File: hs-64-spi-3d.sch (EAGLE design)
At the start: 30 parts, among them J1 DF40C-70DP-0.4V(51), J2 A79622-001, U1 RHD2064_BGA, U2 BNO055, U3 TLV70725

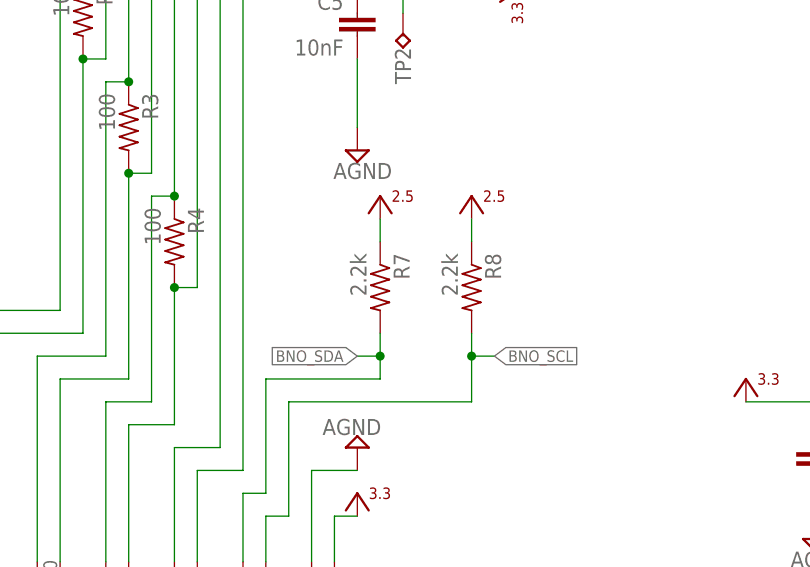
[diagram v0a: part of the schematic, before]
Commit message: Decreased I2C pull-up resistors to 2k.
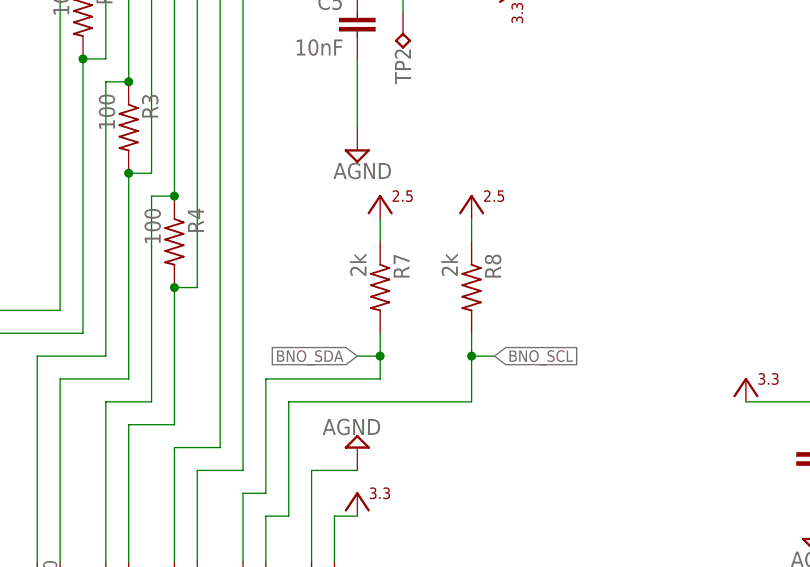
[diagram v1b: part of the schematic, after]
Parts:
- R7, R8: value 2.2k -> 2k
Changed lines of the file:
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@@
 <part name="P7" library="jonnew" deviceset="+3V3" device=""/>
 <part name="U$2" library="jonnew" deviceset="+2V5" device=""/>
-<part name="R7" library="jonnew" deviceset="R" device="_0201T" value="2.2k"/>
-<part name="R8" library="jonnew" deviceset="R" device="_0201T" value="2.2k"/>
+<part name="R7" library="jonnew" deviceset="R" device="_0201T" value="2k"/>
+<part name="R8" library="jonnew" deviceset="R" device="_0201T" value="2k"/>
 <part name="U$3" library="jonnew" deviceset="+2V5" device=""/>
 <part name="U$4" library="jonnew" deviceset="+2V5" device=""/>

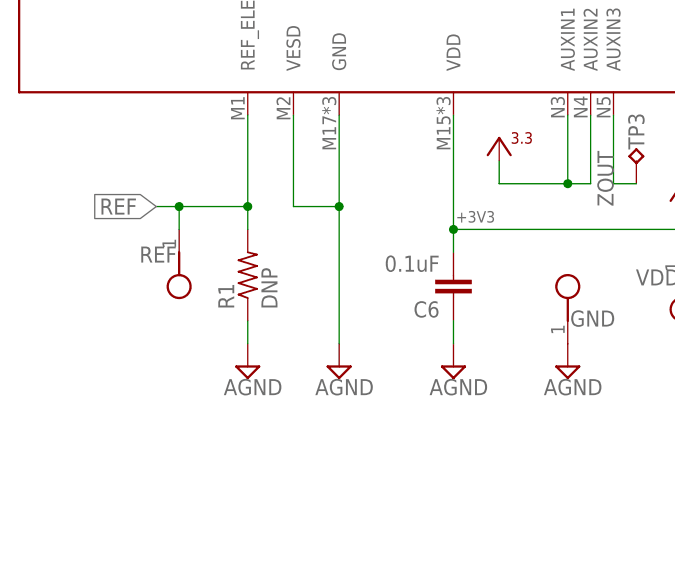
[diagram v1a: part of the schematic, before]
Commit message: Connection between REF to GND is now done by default.
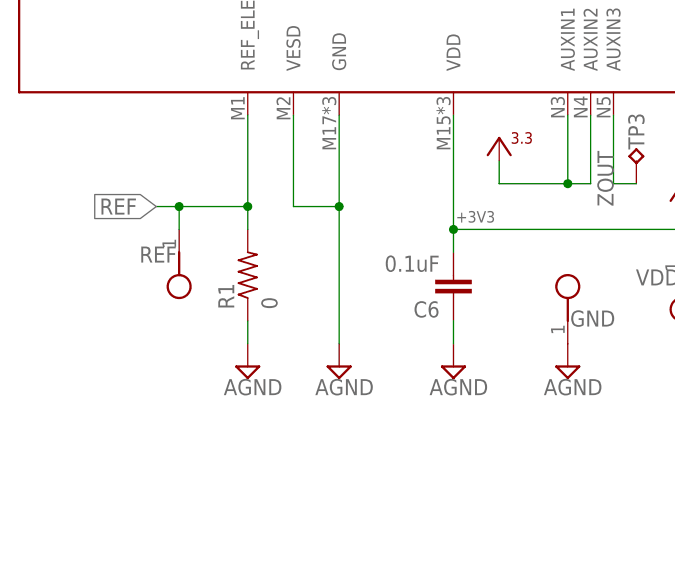
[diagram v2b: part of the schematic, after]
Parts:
- R1: value DNP -> 0
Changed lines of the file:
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@@
 <part name="SUPPLY1" library="jonnew" deviceset="AGND" device=""/>
 <part name="J2" library="hs-64-spi" deviceset="A79622-001" device=""/>
-<part name="R1" library="jonnew" deviceset="R" device="_0603" value="DNP"/>
+<part name="R1" library="jonnew" deviceset="R" device="_0603" value="0"/>
 <part name="SUPPLY11" library="jonnew" deviceset="AGND" device=""/>
 <part name="C7" library="jonnew" deviceset="C" device="_0402" value="1u"/>

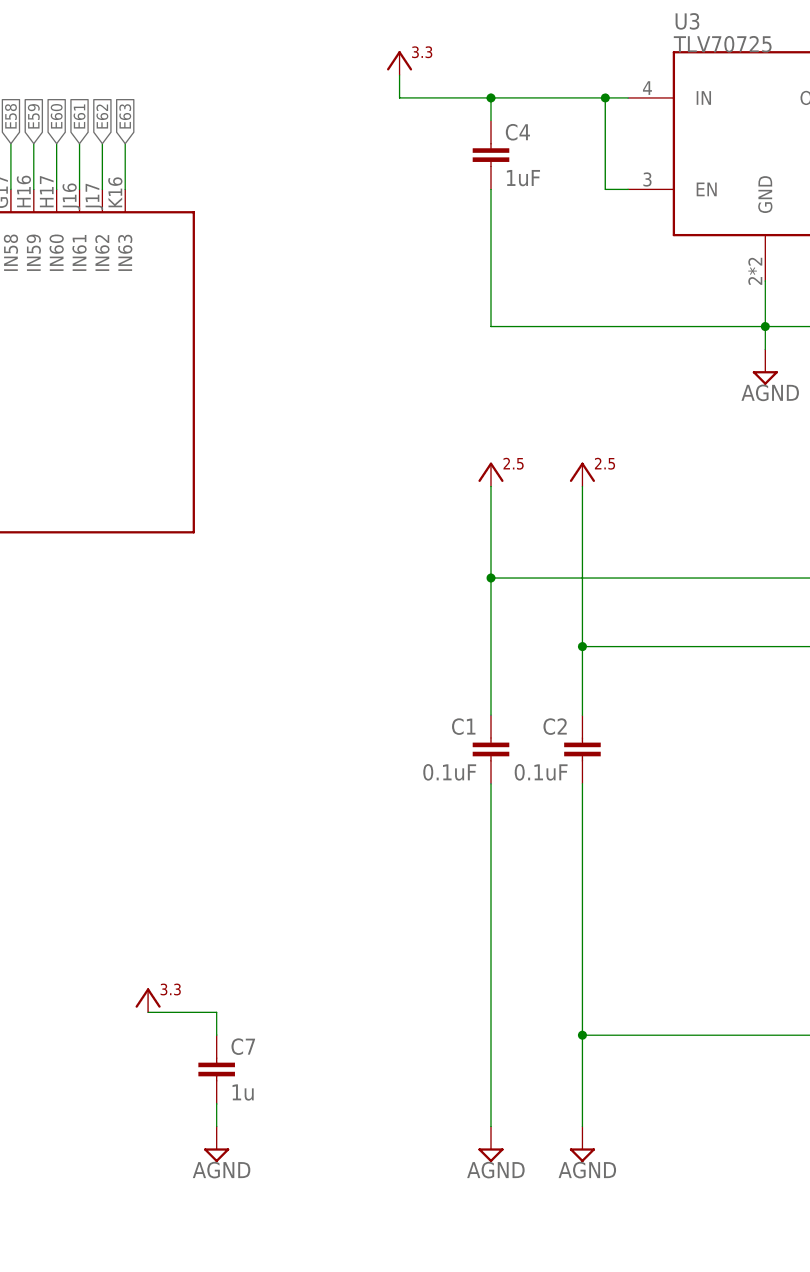
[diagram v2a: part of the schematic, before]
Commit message: Corrected C4 and C7 values to 4.7uF.
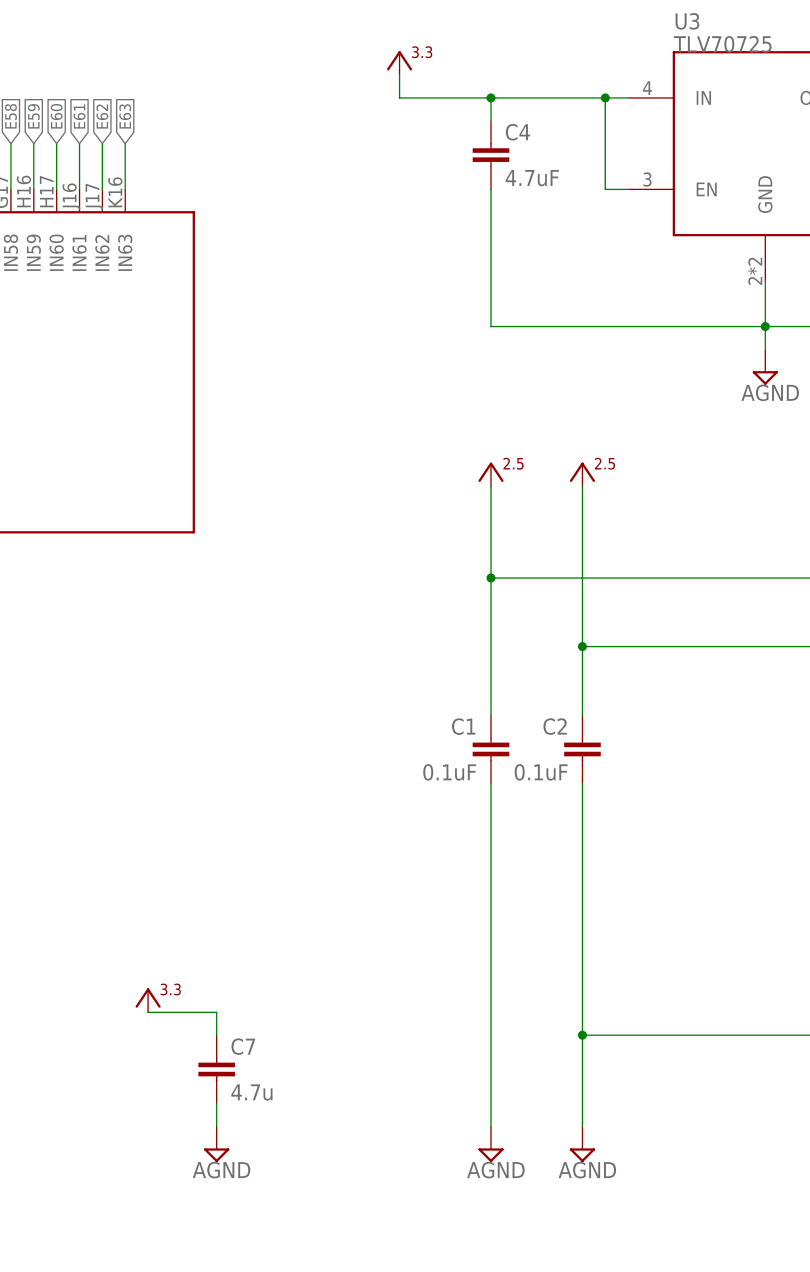
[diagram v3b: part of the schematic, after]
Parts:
- C4: value 1uF -> 4.7uF
- C7: value 1u -> 4.7u
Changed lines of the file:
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@@
 <part name="R1" library="jonnew" deviceset="R" device="_0603" value="0"/>
 <part name="SUPPLY11" library="jonnew" deviceset="AGND" device=""/>
-<part name="C7" library="jonnew" deviceset="C" device="_0402" value="1u"/>
+<part name="C7" library="jonnew" deviceset="C" device="_0402" value="4.7u"/>
 <part name="FRAME1" library="frames" deviceset="A3L-LOC" device=""/>
 <part name="GND" library="RHD2000_eval_board" deviceset="TESTPOINT" device="_SMALL"/>
@@
 <part name="U3" library="jonnew" deviceset="TLV707" device="" value="TLV70725"/>
 <part name="U$45" library="jonnew" deviceset="+2V5" device=""/>
-<part name="C4" library="jonnew" deviceset="C" device="_0402T" value="1uF">
+<part name="C4" library="jonnew" deviceset="C" device="_0402T" value="4.7uF">
 <attribute name="PARTNO" value="CL05A105KO5NNNC"/>
 </part>

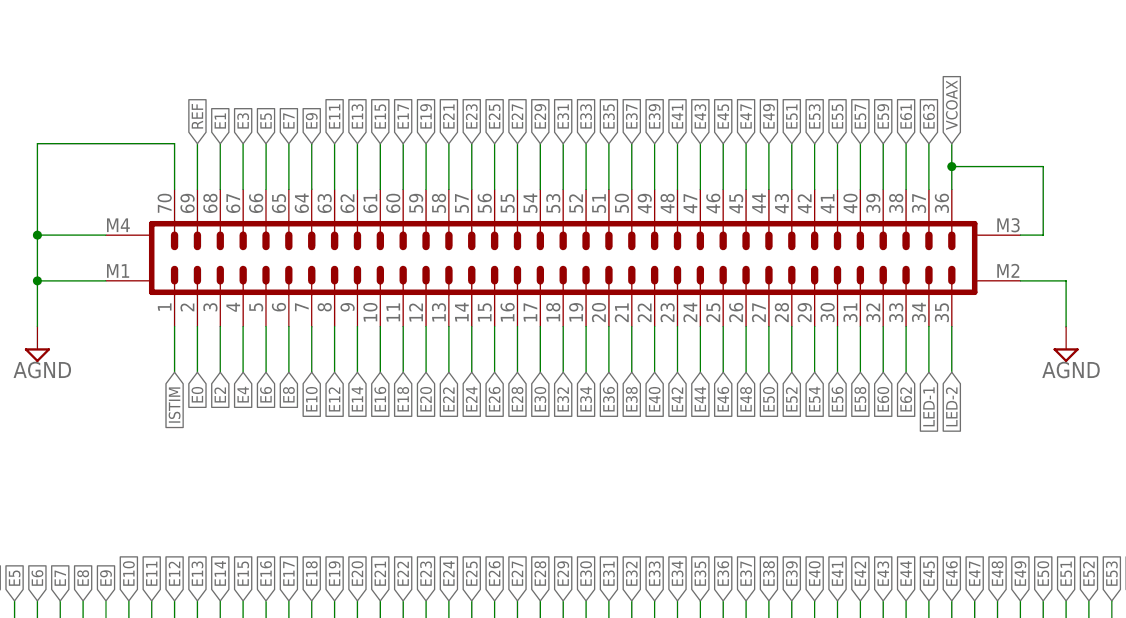
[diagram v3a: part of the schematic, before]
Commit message: Updated Hirose (J1) schematic.
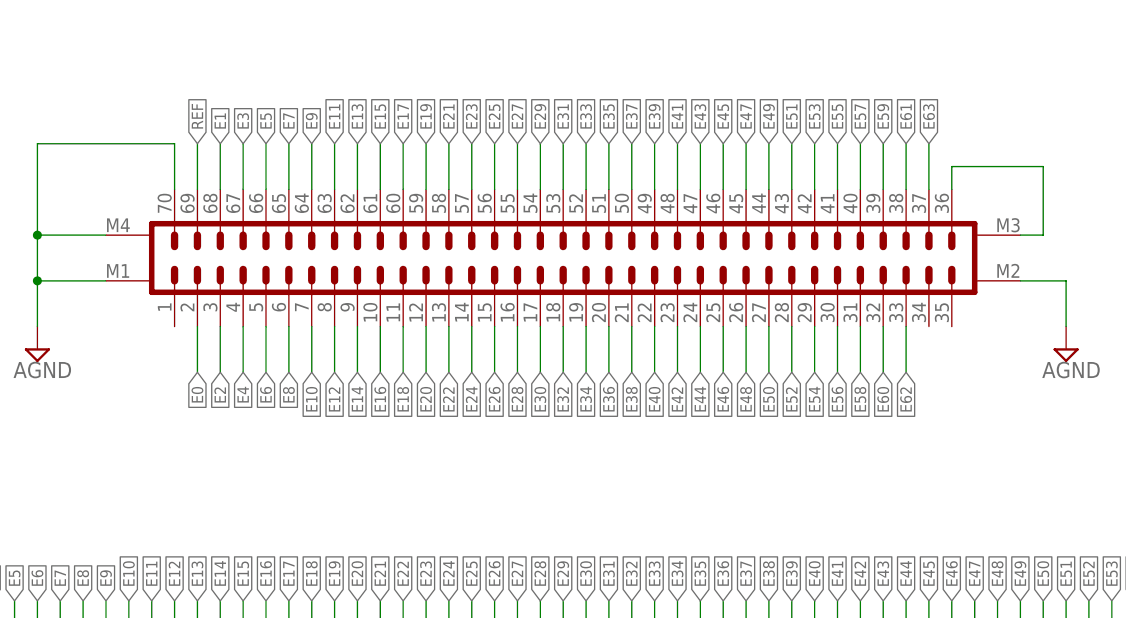
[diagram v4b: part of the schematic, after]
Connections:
- removed net ISTIM: J1.1
- removed net LED-1: J1.34
- removed net LED-2: J1.35
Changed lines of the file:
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@@
 </busses>
 <nets>
-<net name="LED-2" class="0">
-<segment>
-<pinref part="J1" gate="G$1" pin="35"/>
-<wire x1="152.4" y1="200.66" x2="152.4" y2="195.58" width="0.1524" layer="91"/>
-<label x="152.4" y="195.58" size="1.27" layer="95" rot="R270" xref="yes"/>
-</segment>
-</net>
 <net name="VCOAX" class="0">
 <segment>
 <pinref part="J1" gate="G$1" pin="36"/>
 <wire x1="152.4" y1="215.9" x2="152.4" y2="218.44" width="0.1524" layer="91"/>
-<label x="152.4" y="220.98" size="1.27" layer="95" rot="R90" xref="yes"/>
-<wire x1="152.4" y1="218.44" x2="152.4" y2="220.98" width="0.1524" layer="91"/>
 <wire x1="152.4" y1="218.44" x2="162.56" y2="218.44" width="0.1524" layer="91"/>
 <wire x1="162.56" y1="218.44" x2="162.56" y2="210.82" width="0.1524" layer="91"/>
-<junction x="152.4" y="218.44"/>
 <pinref part="J1" gate="G$1" pin="M3"/>
 <wire x1="162.56" y1="210.82" x2="160.02" y2="210.82" width="0.1524" layer="91"/>
@@
 <label x="109.22" y="195.58" size="1.27" layer="95" rot="MR270" xref="yes"/>
 <pinref part="J1" gate="G$1" pin="18"/>
-</segment>
-</net>
-<net name="LED-1" class="0">
-<segment>
-<pinref part="J1" gate="G$1" pin="34"/>
-<wire x1="149.86" y1="195.58" x2="149.86" y2="200.66" width="0.1524" layer="91"/>
-<label x="149.86" y="195.58" size="1.27" layer="95" rot="R270" xref="yes"/>
 </segment>
 </net>
@@
 </segment>
 </net>
-<net name="ISTIM" class="0">
-<segment>
-<pinref part="J1" gate="G$1" pin="1"/>
-<wire x1="66.04" y1="200.66" x2="66.04" y2="195.58" width="0.1524" layer="91"/>
-<label x="66.04" y="195.58" size="1.27" layer="95" rot="R270" xref="yes"/>
-</segment>
-</net>
